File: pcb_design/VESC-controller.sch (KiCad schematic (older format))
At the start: 26 parts, among them J1 GATE_DRIVER_CONN_U, J2 GATE_DRIVER_CONN_V, J3 GATE_DRIVER_CONN_W, J4 micro USB, J5 ACCEL, J6 REGEN, J7 12V, J8 V_BUS, P1 HALL/Encoder, P101 CANBUS, P2 Resolver, P3 PWR_COMM

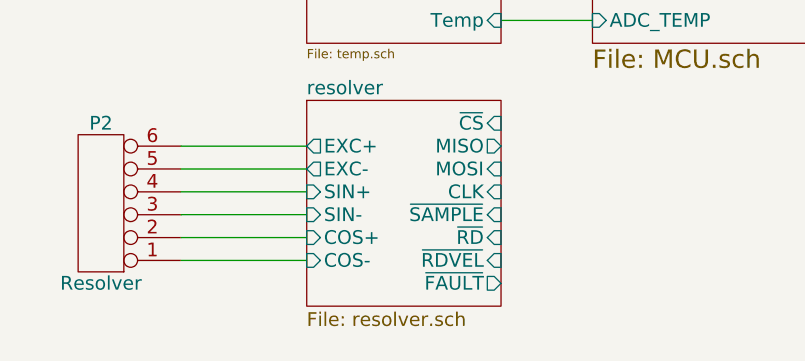
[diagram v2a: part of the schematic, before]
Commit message: Resolver routed using push pull buffer
Signed-off-by: Marcos Chaparro <mchaparro@paltatech.com>
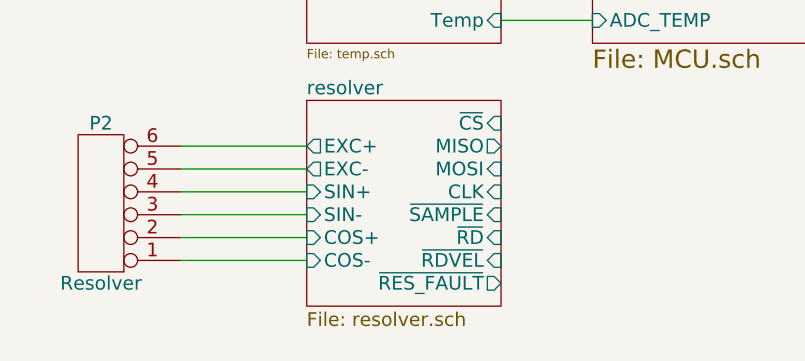
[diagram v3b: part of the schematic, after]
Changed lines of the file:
@@
 $EndComp
 $Comp
-L GND-RESCUE-BLDC_4 #PWR7
+L GND-RESCUE-BLDC_4 #PWR01
 U 1 1 522DA053
 P 1500 4100
-F 0 "#PWR7" H 1500 4100 30  0001 C CNN
+F 0 "#PWR01" H 1500 4100 30  0001 C CNN
 F 1 "GND" H 1500 4030 30  0001 C CNN
 F 2 "" H 1500 4100 60  0001 C CNN
@@
 $EndComp
 $Comp
-L GND-RESCUE-BLDC_4 #PWR5
+L GND-RESCUE-BLDC_4 #PWR02
 U 1 1 522DA0E2
 P 1450 5150
-F 0 "#PWR5" H 1450 5150 30  0001 C CNN
+F 0 "#PWR02" H 1450 5150 30  0001 C CNN
 F 1 "GND" H 1450 5080 30  0001 C CNN
 F 2 "" H 1450 5150 60  0001 C CNN
@@
 $EndComp
 $Comp
-L GND-RESCUE-BLDC_4 #PWR6
+L GND-RESCUE-BLDC_4 #PWR03
 U 1 1 522DA0FC
 P 1500 3150
-F 0 "#PWR6" H 1500 3150 30  0001 C CNN
+F 0 "#PWR03" H 1500 3150 30  0001 C CNN
 F 1 "GND" H 1500 3080 30  0001 C CNN
 F 2 "" H 1500 3150 60  0001 C CNN
@@
 $EndComp
 $Comp
-L GND-RESCUE-BLDC_4 #PWR16
+L GND-RESCUE-BLDC_4 #PWR04
 U 1 1 53FC131A
 P 6600 6000
-F 0 "#PWR16" H 6600 6000 30  0001 C CNN
+F 0 "#PWR04" H 6600 6000 30  0001 C CNN
 F 1 "GND" H 6600 5930 30  0001 C CNN
 F 2 "" H 6600 6000 60  0001 C CNN
@@
 MISO_RX_SCL
 $Comp
-L GND #PWR25
+L GND #PWR05
 U 1 1 58876637
 P 10650 2250
-F 0 "#PWR25" H 10650 2250 30  0001 C CNN
+F 0 "#PWR05" H 10650 2250 30  0001 C CNN
 F 1 "GND" H 10650 2180 30  0001 C CNN
 F 2 "" H 10650 2250 60  0000 C CNN
@@
 	9200 2400 9050 2400
 $Comp
-L GND #PWR18
+L GND #PWR06
 U 1 1 588B9E09
 P 9150 2750
-F 0 "#PWR18" H 9150 2750 30  0001 C CNN
+F 0 "#PWR06" H 9150 2750 30  0001 C CNN
 F 1 "GND" H 9150 2680 30  0001 C CNN
 F 2 "" H 9150 2750 60  0000 C CNN
@@
 	9200 2600 9050 2600
 $Comp
-L GND #PWR27
+L GND #PWR07
 U 1 1 588C277E
 P 10650 3450
-F 0 "#PWR27" H 10650 3450 30  0001 C CNN
+F 0 "#PWR07" H 10650 3450 30  0001 C CNN
 F 1 "GND" H 10650 3380 30  0001 C CNN
 F 2 "" H 10650 3450 60  0000 C CNN
@@
 	9200 3600 9050 3600
 $Comp
-L GND #PWR19
+L GND #PWR08
 U 1 1 588C27A8
 P 9150 3950
-F 0 "#PWR19" H 9150 3950 30  0001 C CNN
+F 0 "#PWR08" H 9150 3950 30  0001 C CNN
 F 1 "GND" H 9150 3880 30  0001 C CNN
 F 2 "" H 9150 3950 60  0000 C CNN
@@
 	8050 4850 7650 4850
 $Comp
-L GND #PWR29
+L GND #PWR09
 U 1 1 588C4E72
 P 10650 4650
-F 0 "#PWR29" H 10650 4650 30  0001 C CNN
+F 0 "#PWR09" H 10650 4650 30  0001 C CNN
 F 1 "GND" H 10650 4580 30  0001 C CNN
 F 2 "" H 10650 4650 60  0000 C CNN
@@
 	9200 4800 9050 4800
 $Comp
-L GND #PWR20
+L GND #PWR010
 U 1 1 588C4E9E
 P 9150 5150
-F 0 "#PWR20" H 9150 5150 30  0001 C CNN
+F 0 "#PWR010" H 9150 5150 30  0001 C CNN
 F 1 "GND" H 9150 5080 30  0001 C CNN
 F 2 "" H 9150 5150 60  0000 C CNN
@@
 	6600 5950 6450 5950
 $Comp
-L GND-RESCUE-BLDC_4 #PWR15
+L GND-RESCUE-BLDC_4 #PWR011
 U 1 1 588CB158
 P 6600 5750
-F 0 "#PWR15" H 6600 5750 30  0001 C CNN
+F 0 "#PWR011" H 6600 5750 30  0001 C CNN
 F 1 "GND" H 6600 5680 30  0001 C CNN
 F 2 "" H 6600 5750 60  0001 C CNN
@@
 $EndComp
 $Comp
-L GND #PWR2
+L GND #PWR012
 U 1 1 588A7EFE
 P 1350 1750
-F 0 "#PWR2" H 1350 1750 30  0001 C CNN
+F 0 "#PWR012" H 1350 1750 30  0001 C CNN
 F 1 "GND" H 1350 1680 30  0001 C CNN
 F 2 "" H 1350 1750 60  0000 C CNN
@@
 	1350 2200 1350 2250
 $Comp
-L GND #PWR4
+L GND #PWR013
 U 1 1 588A9C10
 P 1350 2250
-F 0 "#PWR4" H 1350 2250 30  0001 C CNN
+F 0 "#PWR013" H 1350 2250 30  0001 C CNN
 F 1 "GND" H 1350 2180 30  0001 C CNN
 F 2 "" H 1350 2250 60  0000 C CNN
@@
 	6400 800  6200 800
 $Comp
-L GND #PWR14
+L GND #PWR014
 U 1 1 588CC018
 P 6250 950
-F 0 "#PWR14" H 6250 950 30  0001 C CNN
+F 0 "#PWR014" H 6250 950 30  0001 C CNN
 F 1 "GND" H 6250 880 30  0001 C CNN
 F 2 "" H 6250 950 60  0000 C CNN
@@
 	6250 900  6200 900
 $Comp
-L +5 #PWR1
+L +5 #PWR015
 U 1 1 588B45C6
 P 1350 1500
-F 0 "#PWR1" H 250 -150 30  0001 C CNN
+F 0 "#PWR015" H 250 -150 30  0001 C CNN
 F 1 "+5" H 1350 1600 50  0000 C CNN
 F 2 "" H 250 -200 60  0000 C CNN
@@
 	1300 1500 1450 1500
 $Comp
-L +5 #PWR3
+L +5 #PWR016
 U 1 1 588B5F6B
 P 1350 2000
-F 0 "#PWR3" H 250 350 30  0001 C CNN
+F 0 "#PWR016" H 250 350 30  0001 C CNN
 F 1 "+5" H 1350 2100 50  0000 C CNN
 F 2 "" H 250 300 60  0000 C CNN
@@
 	1300 2000 1450 2000
 $Comp
-L +5 #PWR13
+L +5 #PWR017
 U 1 1 588BB3A4
 P 2800 2650
-F 0 "#PWR13" H 1700 1000 30  0001 C CNN
+F 0 "#PWR017" H 1700 1000 30  0001 C CNN
 F 1 "+5" H 2800 2750 50  0000 C CNN
 F 2 "" H 1700 950 60  0000 C CNN
@@
 $EndComp
 $Comp
-L +5 #PWR9
+L +5 #PWR018
 U 1 1 588BE146
 P 1550 4950
-F 0 "#PWR9" H -50 -250 30  0001 C CNN
+F 0 "#PWR018" H -50 -250 30  0001 C CNN
 F 1 "+5" H 1550 5050 50  0000 C CNN
 F 2 "" H -50 -300 60  0000 C CNN
@@
 $EndComp
 $Comp
-L +3.3 #PWR12
+L +3.3 #PWR019
 U 1 1 588BE494
 P 1700 5050
-F 0 "#PWR12" H 50  -200 30  0001 C CNN
+F 0 "#PWR019" H 50  -200 30  0001 C CNN
 F 1 "+3.3" H 1700 5150 50  0000 C CNN
 F 2 "" H 50  -250 60  0000 C CNN
@@
 $EndComp
 $Comp
-L +5 #PWR8
+L +5 #PWR020
 U 1 1 588C053A
 P 1500 4600
-F 0 "#PWR8" H -100 -600 30  0001 C CNN
+F 0 "#PWR020" H -100 -600 30  0001 C CNN
 F 1 "+5" H 1500 4700 50  0000 C CNN
 F 2 "" H -100 -650 60  0000 C CNN
@@
 	1500 4600 1450 4600
 $Comp
-L +24 #PWR17
+L +24 #PWR021
 U 1 1 588CE8C9
 P 7800 800
-F 0 "#PWR17" H -650 -50 30  0001 C CNN
+F 0 "#PWR021" H -650 -50 30  0001 C CNN
 F 1 "+24" H 7800 933 50  0000 C CNN
 F 2 "" H -650 -100 60  0000 C CNN
@@
 $EndComp
 $Comp
-L +24 #PWR24
+L +24 #PWR022
 U 1 1 588D0DE1
 P 10650 2000
-F 0 "#PWR24" H 10700 2050 30  0001 C CNN
+F 0 "#PWR022" H 10700 2050 30  0001 C CNN
 F 1 "+24" H 10650 2133 50  0000 C CNN
 F 2 "" H -50 -300 60  0000 C CNN
@@
 $EndComp
 $Comp
-L +24 #PWR26
+L +24 #PWR023
 U 1 1 588D1EB4
 P 10650 3200
-F 0 "#PWR26" H 10700 3250 30  0001 C CNN
+F 0 "#PWR023" H 10700 3250 30  0001 C CNN
 F 1 "+24" H 10650 3333 50  0000 C CNN
 F 2 "" H -50 -250 60  0000 C CNN
@@
 $EndComp
 $Comp
-L +24 #PWR28
+L +24 #PWR024
 U 1 1 588D2D5A
 P 10650 4400
-F 0 "#PWR28" H 10700 4450 30  0001 C CNN
+F 0 "#PWR024" H 10700 4450 30  0001 C CNN
 F 1 "+24" H 10650 4533 50  0000 C CNN
 F 2 "" H -50 -300 60  0000 C CNN
@@
 	9800 5750 9050 5750
 $Comp
-L GND #PWR23
+L GND #PWR025
 U 1 1 588E5603
 P 9750 5900
-F 0 "#PWR23" H 9800 5950 30  0001 C CNN
+F 0 "#PWR025" H 9800 5950 30  0001 C CNN
 F 1 "GND" H 0   -270 30  0001 C CNN
 F 2 "" H 0   -200 60  0000 C CNN
@@
 	9750 5850 9800 5850
 $Comp
-L +5 #PWR22
+L +5 #PWR026
 U 1 1 588E703F
 P 9750 5550
-F 0 "#PWR22" H 8650 3900 30  0001 C CNN
+F 0 "#PWR026" H 8650 3900 30  0001 C CNN
 F 1 "+5" H 9750 5650 50  0000 C CNN
 F 2 "" H 8650 3850 60  0000 C CNN
@@
 $EndComp
 $Comp
-L GND #PWR21
+L GND #PWR027
 U 1 1 588D02C2
 P 9450 5550
-F 0 "#PWR21" H 9500 5600 30  0001 C CNN
+F 0 "#PWR027" H 9500 5600 30  0001 C CNN
 F 1 "GND" H -300 -620 30  0001 C CNN
 F 2 "" H -300 -550 60  0000 C CNN
@@
 $EndComp
 $Comp
-L GND #PWR10
+L GND #PWR028
 U 1 1 588DFDA4
 P 1650 1500
-F 0 "#PWR10" H 1650 1500 30  0001 C CNN
+F 0 "#PWR028" H 1650 1500 30  0001 C CNN
 F 1 "GND" H 1650 1430 30  0001 C CNN
 F 2 "" H 1650 1500 60  0000 C CNN
@@
 Connection ~ 1350 2000
 $Comp
-L GND #PWR11
+L GND #PWR029
 U 1 1 588E1A2D
 P 1650 2000
-F 0 "#PWR11" H 1650 2000 30  0001 C CNN
+F 0 "#PWR029" H 1650 2000 30  0001 C CNN
 F 1 "GND" H 1650 1930 30  0001 C CNN
 F 2 "" H 1650 2000 60  0000 C CNN
@@
 F13 "~RD" I R 2850 6900 60
 F14 "~RDVEL" I R 2850 7000 60
-F15 "~FAULT" O R 2850 7100 60
+F15 "~RES_FAULT" O R 2850 7100 60
 $EndSheet
 Wire Wire Line
